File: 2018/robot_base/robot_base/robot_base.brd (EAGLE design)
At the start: 81 x 72.4 mm, 38 parts

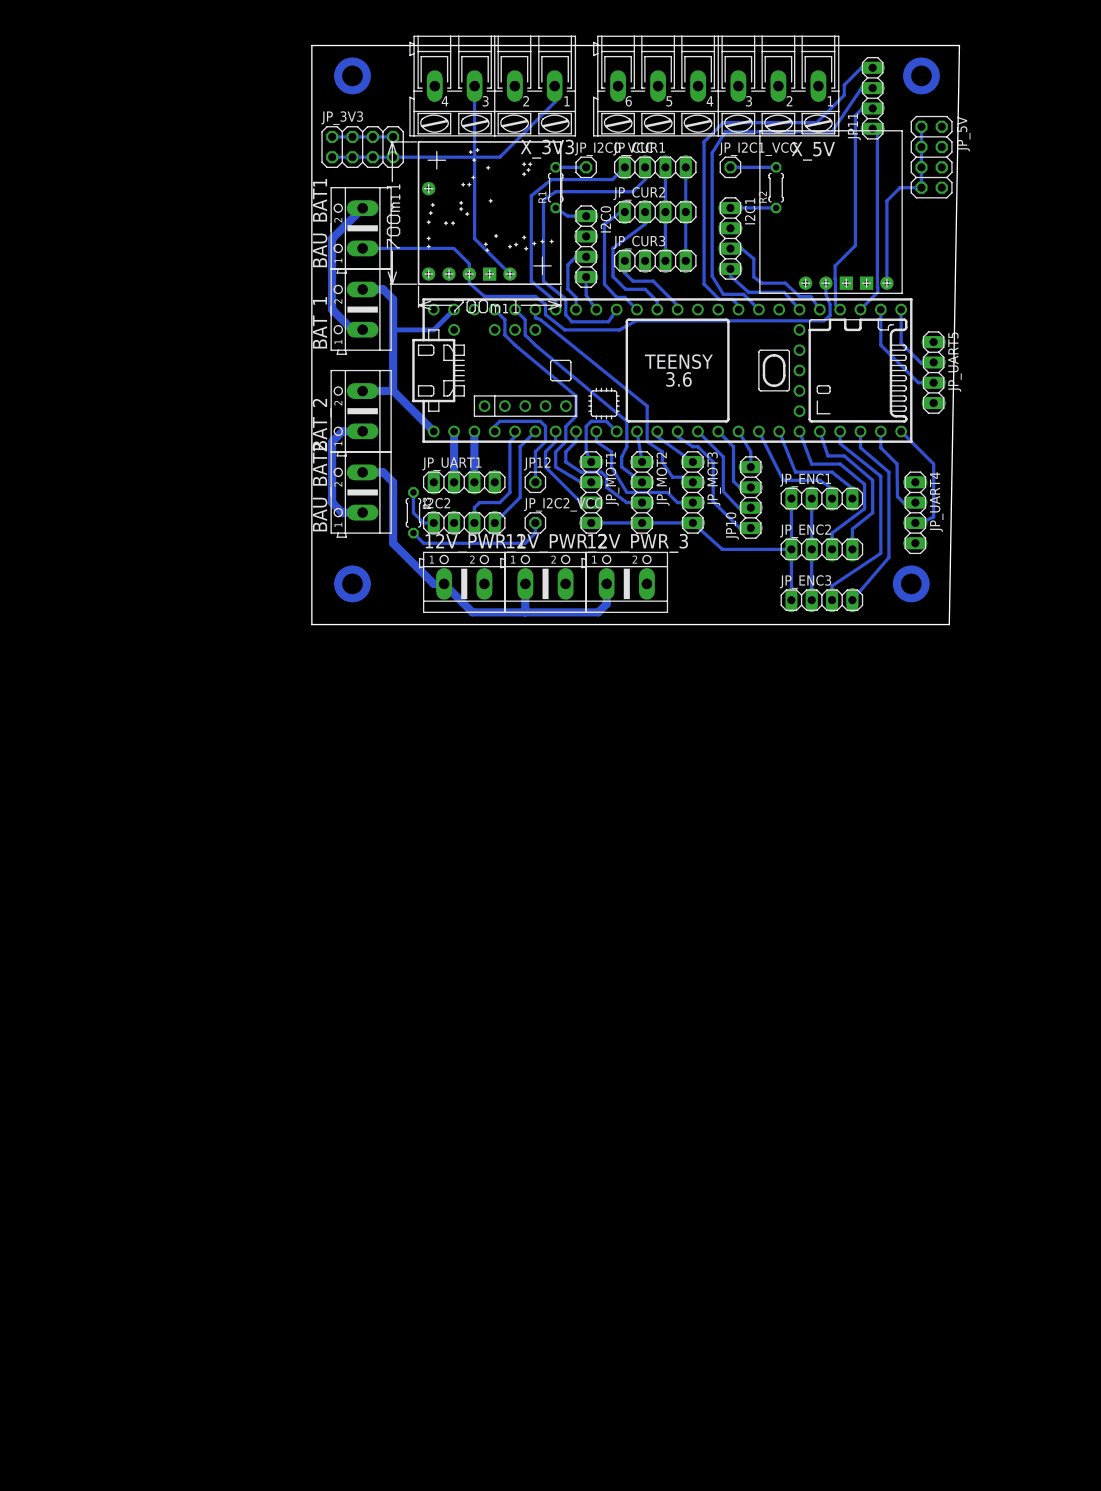
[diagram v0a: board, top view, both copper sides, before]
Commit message: Changed I2C Pull-Up resistor selector to match I2C specifications
Note: I2C Resistors doesn't have any value yet. Assessment of line
capacitance is in progress...
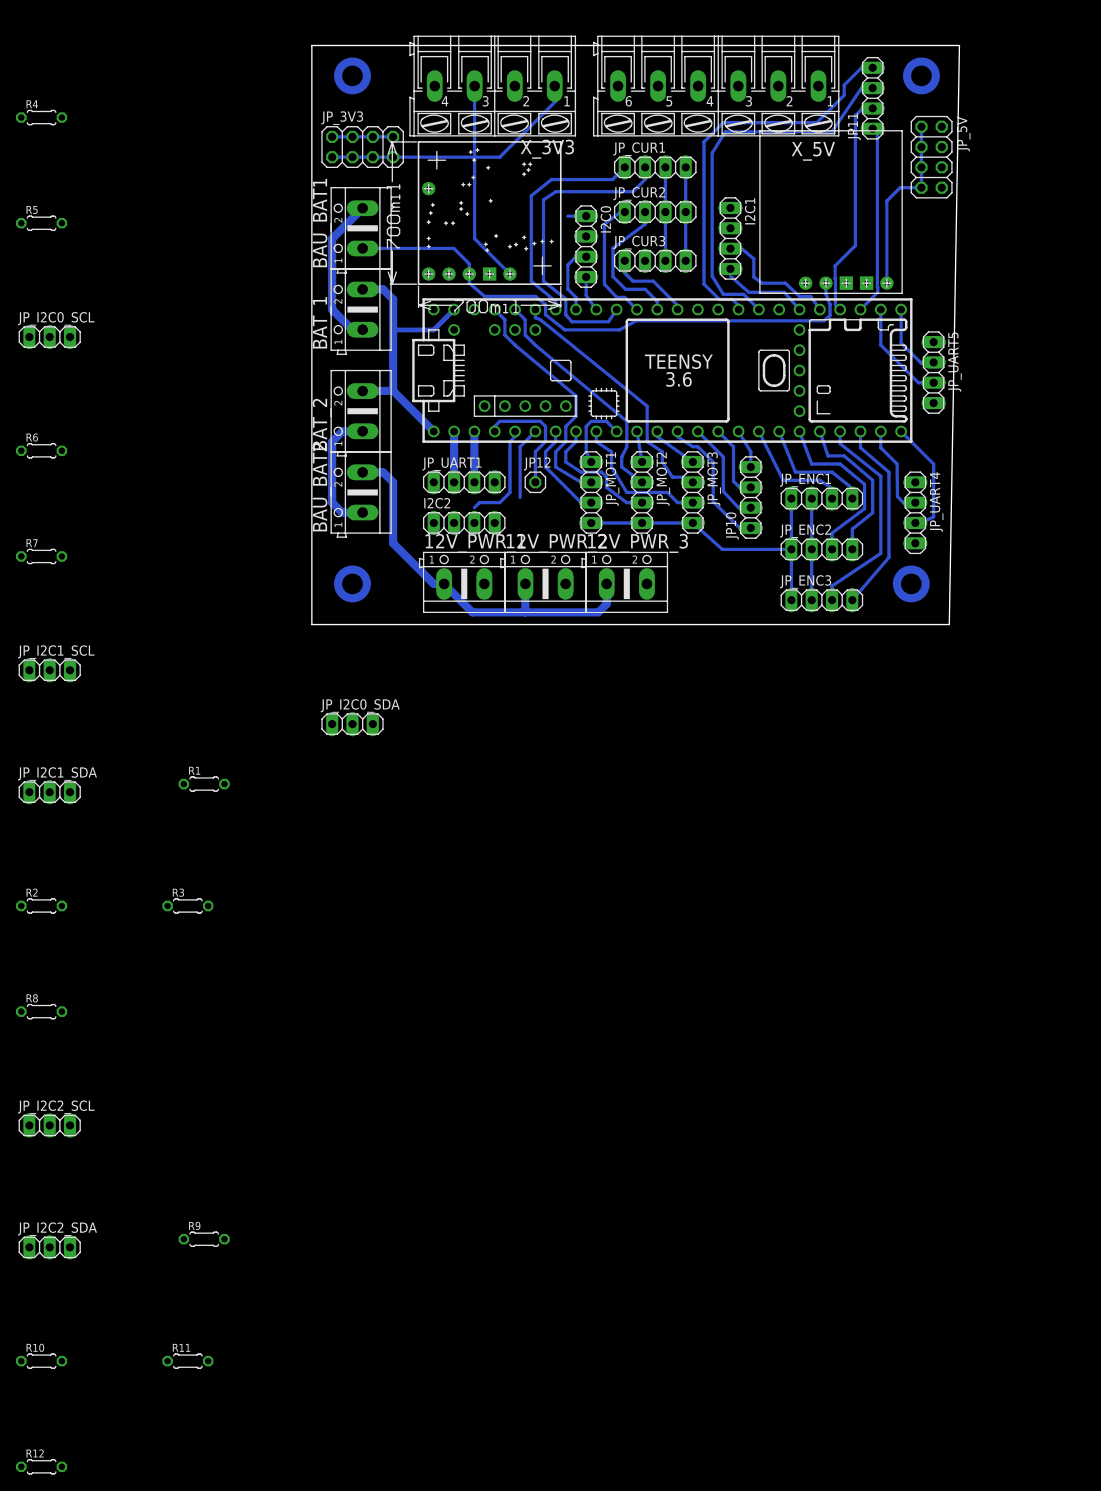
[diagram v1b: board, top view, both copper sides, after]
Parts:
- removed JP_I2C0_VCC, JP_I2C1_VCC, JP_I2C2_VCC: (no value), pinhead:1X01
- added JP_I2C0_SCL, JP_I2C0_SDA, JP_I2C1_SCL, JP_I2C1_SDA, JP_I2C2_SCL, JP_I2C2_SDA: (no value), pinhead:1X03
- added R10, R11, R12, R4, R5, R6, R7, R8, R9: (no value), rcl:0204/5
- moved R2 128.4 mm to (-23.6, -33.9), turned to 0 degrees
- moved R1 86.5 mm to (-3.30, -18.7), turned to 0 degrees
- moved R3 56.7 mm to (-5.33, -33.9), turned to 0 degrees
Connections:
- removed net I2C1_VCC: I2C1.1, R2.1
- removed net I2C2_VCC: I2C2.1, R3.1
- new net N$12: JP_I2C0_SDA.1, R4.2
- new net N$13: JP_I2C0_SDA.3, R5.1
- new net N$14: JP_I2C0_SCL.1, R6.2
- new net N$15: JP_I2C0_SCL.3, R7.1
- new net N$16: JP_I2C1_SCL.3, R8.1
- new net N$17: JP_I2C2_SDA.1, R9.2
- new net N$18: JP_I2C2_SDA.3, R10.1
- new net N$19: JP_I2C2_SCL.1, R11.2
- new net N$20: JP_I2C2_SCL.3, R12.1
- net 3V3: now also R10.2, R12.2, R2.2, R5.2, R7.2, R8.2
- net 5V: now also R1.1, R11.1, R3.1, R4.1, R6.1, R9.1
- net I2C0_VCC: now also I2C1.1, I2C2.1; no longer R1.1
- net N$10: now also JP_I2C1_SDA.3, R2.1; no longer JP_I2C1_VCC.1, R2.2
- net N$11: now also JP_I2C1_SCL.1; no longer JP_I2C2_VCC.1
- net N$9: now also JP_I2C1_SDA.1; no longer JP_I2C0_VCC.1
- net SCL0: now also I2C1.3, I2C2.3, JP_I2C0_SCL.2, JP_I2C1_SCL.2, JP_I2C2_SCL.2
- net SCL1: no longer I2C1.3
- net SCL2: no longer I2C2.3
- net SDA0: now also I2C1.4, I2C2.4, JP_I2C0_SDA.2, JP_I2C1_SDA.2, JP_I2C2_SDA.2
- net SDA1: no longer I2C1.4
- net SDA2: no longer I2C2.4
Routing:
- net N$11: track 17.6 -> 0.00 mm
- net N$10: track 5.71 -> 0.00 mm
- net I2C1_VCC: track 5.71 -> 0.00 mm
- net I2C2_VCC: track 5.61 -> 0.00 mm
- net SDA2: track 13.5 -> 9.04 mm
- net N$9: track 3.81 -> 0.00 mm
- net SCL2: track 15.0 -> 13.1 mm
- net I2C0_VCC: track 4.12 -> 2.29 mm
- net SCL1: track 15.7 -> 14.3 mm
- net SDA1: track 11.3 -> 10.4 mm

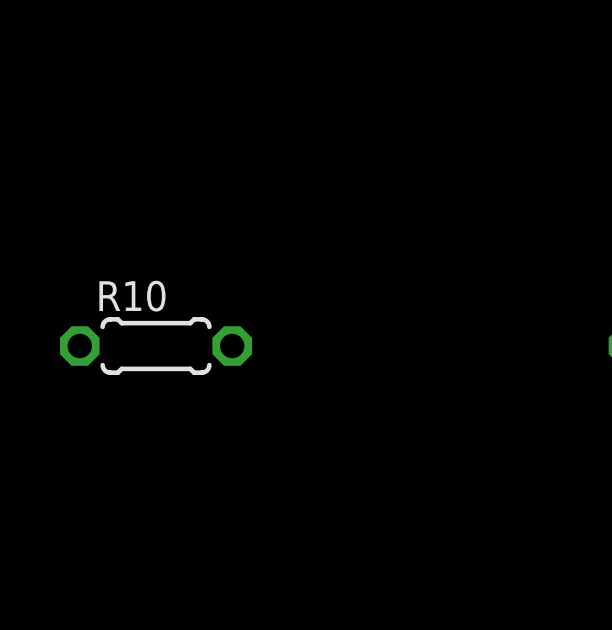
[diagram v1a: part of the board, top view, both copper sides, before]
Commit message: Updated I2C ports and pull-up system to match I2C standard specifications
Note : Assessment of Pull-Up resistors values is still pending.
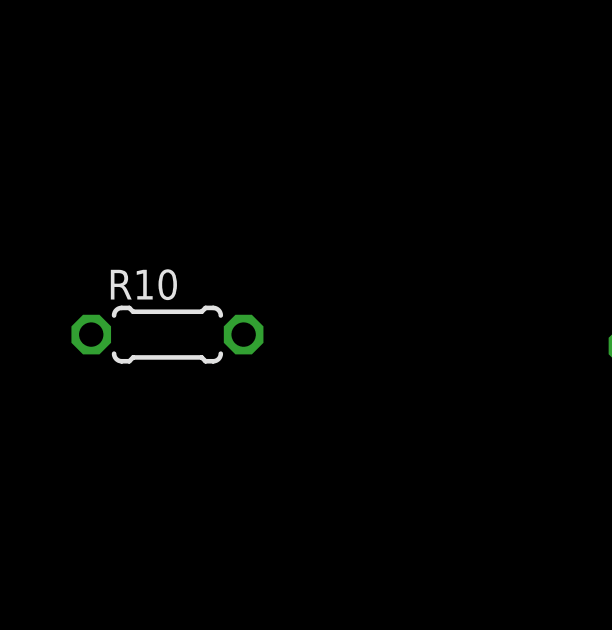
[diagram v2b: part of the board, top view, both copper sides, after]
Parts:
- moved R10 0.54 mm to (-23.2, -90.4)
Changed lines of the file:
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@@
 <element name="JP_I2C2_SDA" library="pinhead" library_urn="urn:adsk.eagle:library:325" package="1X03" package3d_urn="urn:adsk.eagle:package:22458/2" value="" x="-22.606" y="-76.581"/>
 <element name="R9" library="rcl" library_urn="urn:adsk.eagle:library:334" package="0204/5" package3d_urn="urn:adsk.eagle:package:23488/1" value="" x="-3.302" y="-75.565"/>
-<element name="R10" library="rcl" library_urn="urn:adsk.eagle:library:334" package="0204/5" package3d_urn="urn:adsk.eagle:package:23488/1" value="" x="-23.622" y="-90.805"/>
+<element name="R10" library="rcl" library_urn="urn:adsk.eagle:library:334" package="0204/5" package3d_urn="urn:adsk.eagle:package:23488/1" value="" x="-23.241" y="-90.424"/>
 <element name="JP_I2C2_SCL" library="pinhead" library_urn="urn:adsk.eagle:library:325" package="1X03" package3d_urn="urn:adsk.eagle:package:22458/2" value="" x="-22.606" y="-61.341"/>
 <element name="R11" library="rcl" library_urn="urn:adsk.eagle:library:334" package="0204/5" package3d_urn="urn:adsk.eagle:package:23488/1" value="" x="-5.334" y="-90.805"/>
@@
 <contactref element="R10" pad="2"/>
 <contactref element="R12" pad="2"/>
-<wire x1="-21.082" y1="-90.805" x2="-21.082" y2="-104.013" width="0" layer="19" extent="1-1"/>
-<wire x1="-21.082" y1="-47.117" x2="-21.082" y2="-90.805" width="0" layer="19" extent="1-1"/>
+<wire x1="-20.701" y1="-90.424" x2="-21.082" y2="-104.013" width="0" layer="19" extent="1-1"/>
+<wire x1="-21.082" y1="-47.117" x2="-20.701" y2="-90.424" width="0" layer="19" extent="1-1"/>
 <wire x1="-21.082" y1="-33.909" x2="-21.082" y2="-47.117" width="0" layer="19" extent="1-1"/>
 <wire x1="-21.082" y1="9.779" x2="-21.082" y2="-33.909" width="0" layer="19" extent="1-1"/>
@@
 <contactref element="JP_I2C2_SDA" pad="3"/>
 <contactref element="R10" pad="1"/>
-<wire x1="-20.066" y1="-76.581" x2="-26.162" y2="-90.805" width="0" layer="19" extent="1-1"/>
+<wire x1="-20.066" y1="-76.581" x2="-25.781" y2="-90.424" width="0" layer="19" extent="1-1"/>
 </signal>
 <signal name="N$19">

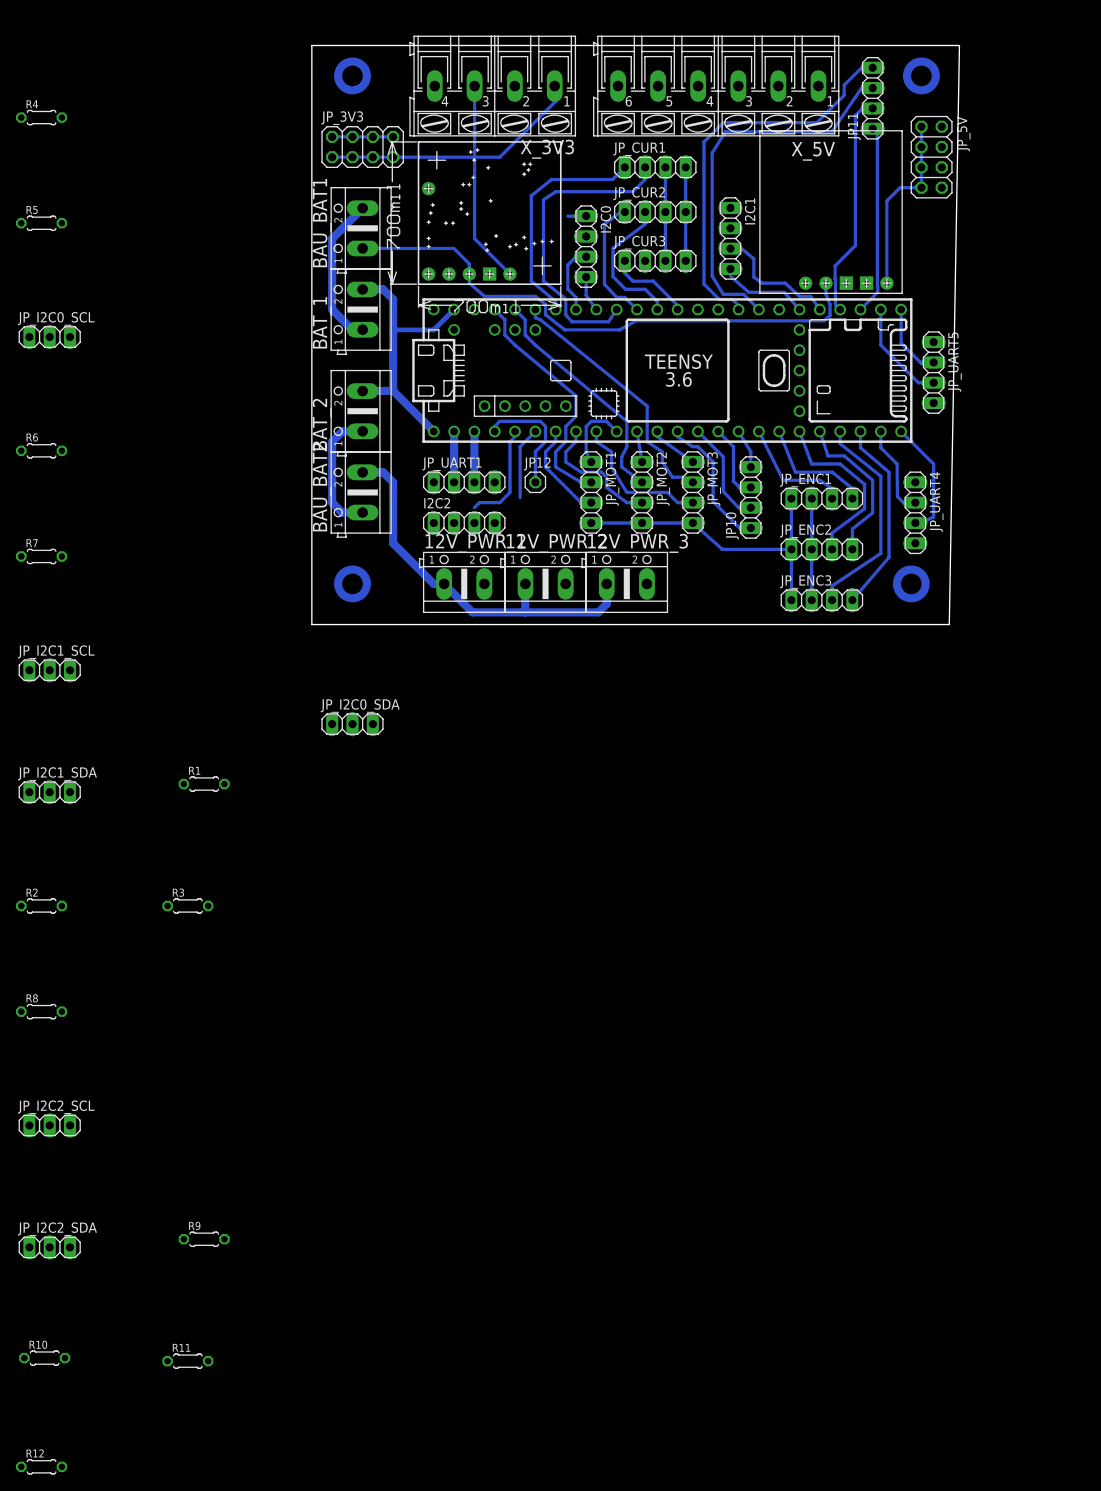
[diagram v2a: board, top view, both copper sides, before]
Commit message: Simplified i2c pull-up selector and Partial routing (77%)
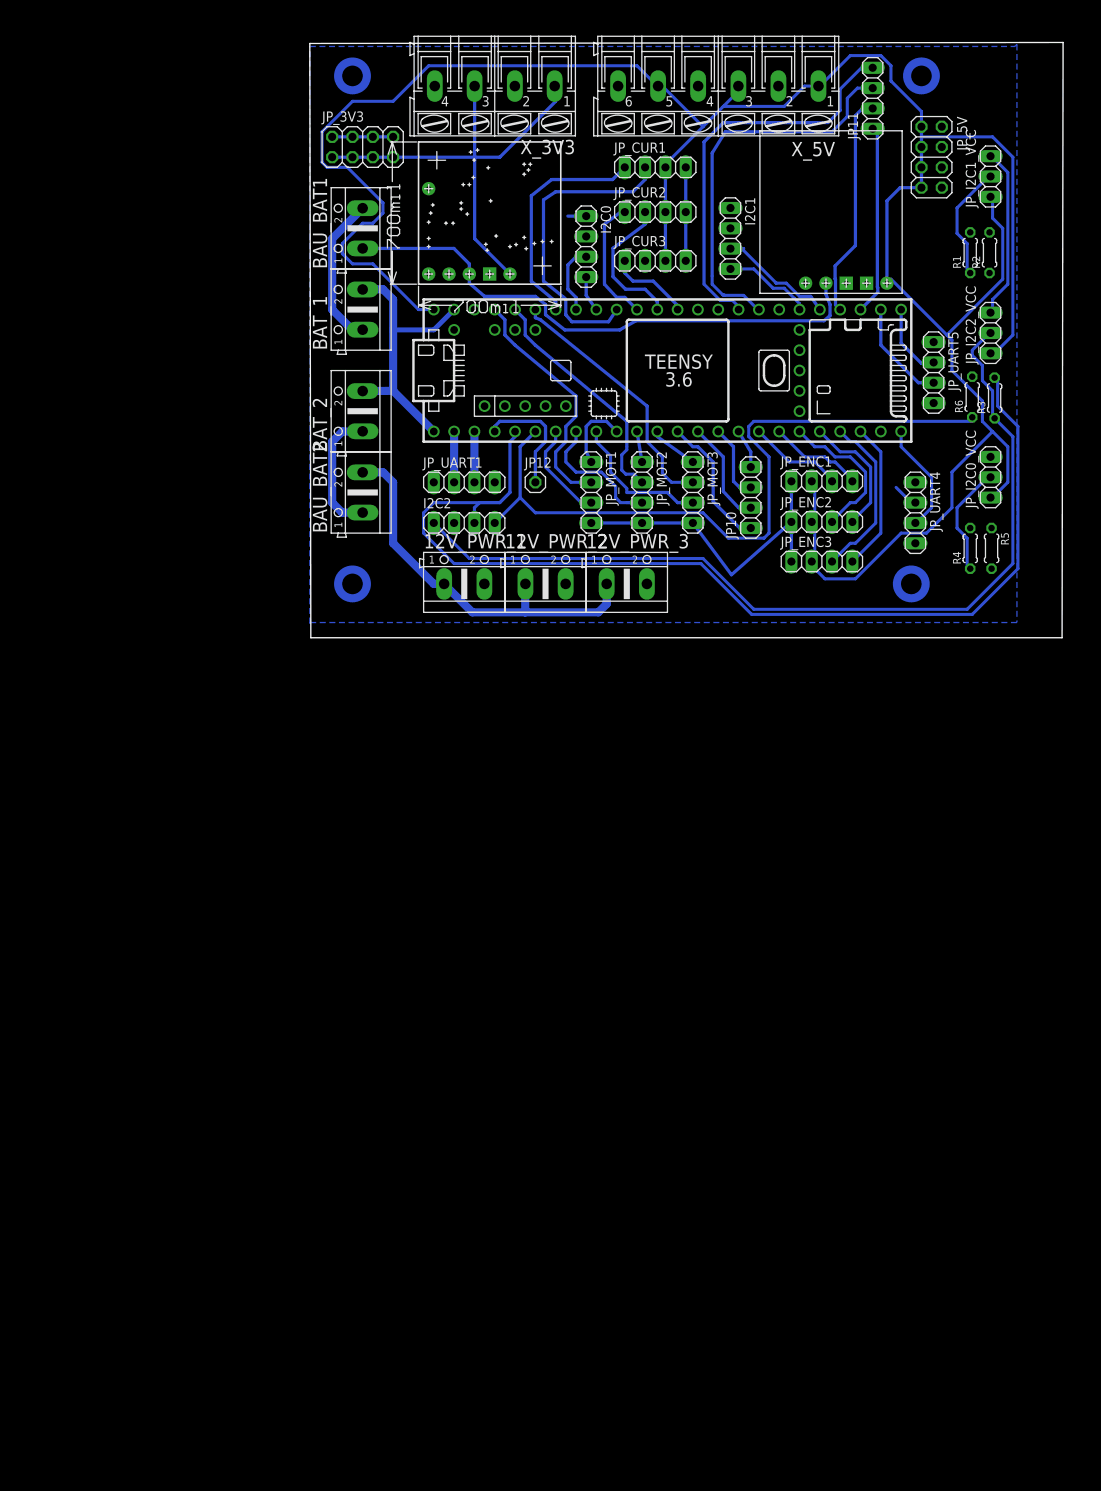
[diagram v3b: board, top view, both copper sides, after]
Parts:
- removed JP_I2C0_SCL, JP_I2C0_SDA, JP_I2C1_SCL, JP_I2C1_SDA, JP_I2C2_SCL, JP_I2C2_SDA: (no value), pinhead:1X03
- removed R10, R11, R12, R7, R8, R9: (no value), rcl:0204/5
- added JP_I2C0_VCC, JP_I2C1_VCC, JP_I2C2_VCC: (no value), pinhead:1X03
- moved R2 143.9 mm to (94.9, 47.8), turned to 90 degrees
- moved R4 128.0 mm to (92.5, 10.8), turned to 90 degrees
- moved R5 125.5 mm to (95.1, 10.8), turned to 270 degrees
- moved R3 119.2 mm to (95.5, 29.6), turned to 90 degrees
- moved R1 116.5 mm to (92.5, 47.8), turned to 90 degrees
- moved R6 116.5 mm to (92.7, 29.7), turned to 90 degrees
- moved JP_ENC3 4.83 mm to (73.9, 9.14)
- moved JP_ENC2 3.43 mm to (73.9, 14.1)
- moved JP_ENC1 2.16 mm to (73.9, 19.2)
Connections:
- removed net N$10: JP_I2C1_SDA.3, R2.1
- removed net N$11: JP_I2C1_SCL.1, R3.2
- removed net N$12: JP_I2C0_SDA.1, R4.2
- removed net N$13: JP_I2C0_SDA.3, R5.1
- removed net N$14: JP_I2C0_SCL.1, R6.2
- removed net N$15: JP_I2C0_SCL.3, R7.1
- removed net N$16: JP_I2C1_SCL.3, R8.1
- removed net N$17: JP_I2C2_SDA.1, R9.2
- removed net N$18: JP_I2C2_SDA.3, R10.1
- removed net N$19: JP_I2C2_SCL.1, R11.2
- removed net N$20: JP_I2C2_SCL.3, R12.1
- removed net N$9: JP_I2C1_SDA.1, R1.2
- new net I2C1_VCC: I2C1.1, JP_I2C1_VCC.2, R1.1
- new net I2C2_VCC: I2C2.1, JP_I2C2_VCC.2, R3.1
- net 3V3: now also JP_I2C0_VCC.3, JP_I2C1_VCC.3, JP_I2C2_VCC.3; no longer R10.2, R12.2, R2.2, R5.2, R7.2, R8.2
- net 5V: now also JP_I2C0_VCC.1, JP_I2C1_VCC.1, JP_I2C2_VCC.1; no longer R1.1, R11.1, R3.1, R4.1, R6.1, R9.1
- net I2C0_VCC: now also JP_I2C0_VCC.2, R4.1; no longer I2C1.1, I2C2.1
- net SCL0: now also R4.2; no longer I2C1.3, I2C2.3, JP_I2C0_SCL.2, JP_I2C1_SCL.2, JP_I2C2_SCL.2
- net SCL1: now also I2C1.3, R1.2
- net SCL2: now also I2C2.3, R3.2
- net SDA0: now also R5.1; no longer I2C1.4, I2C2.4, JP_I2C0_SDA.2, JP_I2C1_SDA.2, JP_I2C2_SDA.2
- net SDA1: now also I2C1.4, R2.1
- net SDA2: now also I2C2.4, R6.1
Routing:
- net 5V: track 47.3 -> 313.4 mm
- net SCL2: track 13.1 -> 131.0 mm
- net I2C2_VCC: track 0.00 -> 111.2 mm
- net SDA2: track 9.04 -> 90.1 mm
- net 3V3: track 58.1 -> 79.5 mm
- net I2C1_VCC: track 0.00 -> 14.6 mm
- net I2C0_VCC: track 2.29 -> 16.6 mm
- net RX4: track 11.7 -> 3.20 mm
- net ENC3_A: track 26.8 -> 21.1 mm
- net ENC3_B: track 24.4 -> 18.8 mm
- net ENC2_B: track 19.8 -> 16.0 mm
- net ENC2_A: track 22.0 -> 18.7 mm
- net ENC1_B: track 14.6 -> 11.8 mm
- net ENC1_A: track 14.5 -> 11.8 mm
- net GND: track 93.7 -> 95.5 mm
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- added copper zone on layer 16, net GND
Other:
- board size 81 x 72.4 mm -> 94.2 x 74.4 mm
